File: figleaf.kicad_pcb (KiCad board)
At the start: 2 copper layers, 145 x 105 mm, 70 parts, among them J1 Conn_01x02_Pin, J2 HRO_TYPE-C-31-M-14, J3 Battery, J9 TC2030_SWD, Q2 2N7002, SW1 PWR, SW2 RST, U1 SRV05-4, U10 MAX17048, U3 BQ24075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

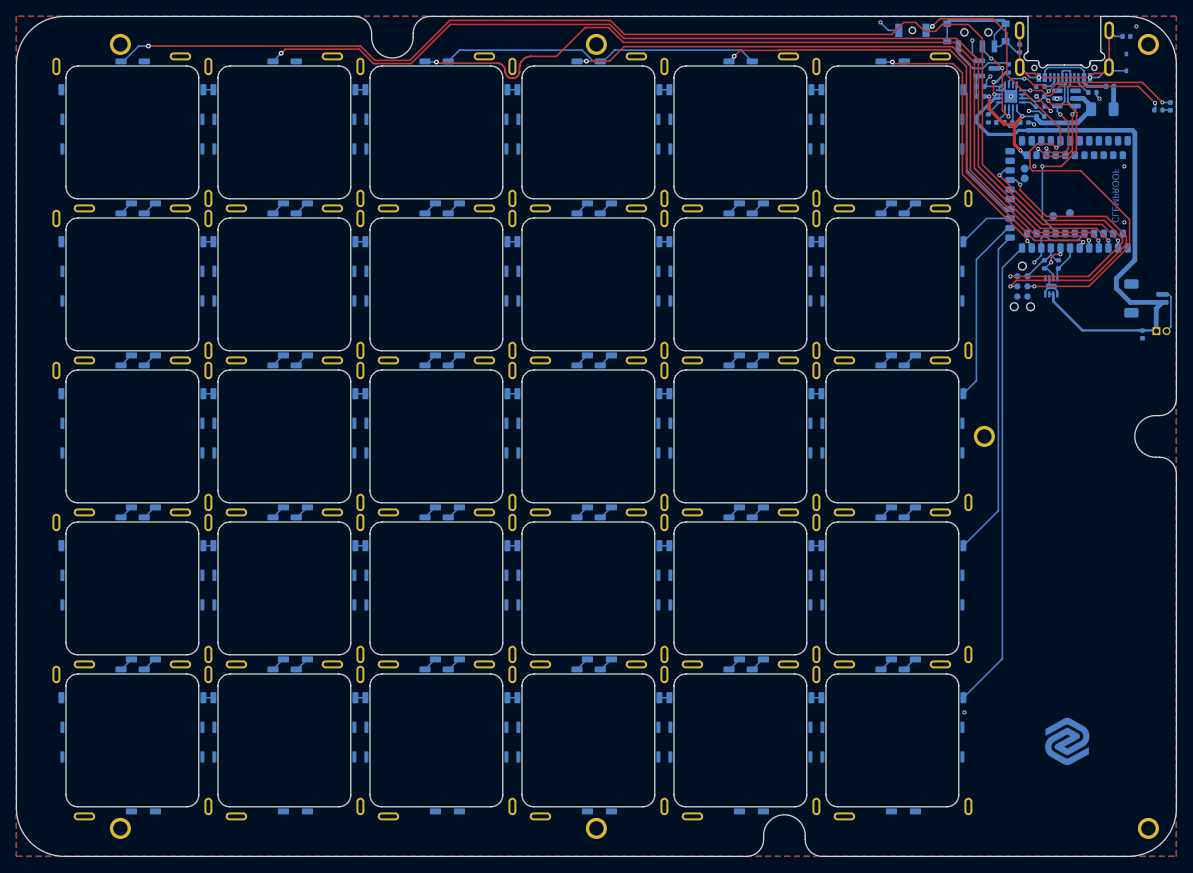
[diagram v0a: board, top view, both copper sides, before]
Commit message: data line thickness + mounting cuts
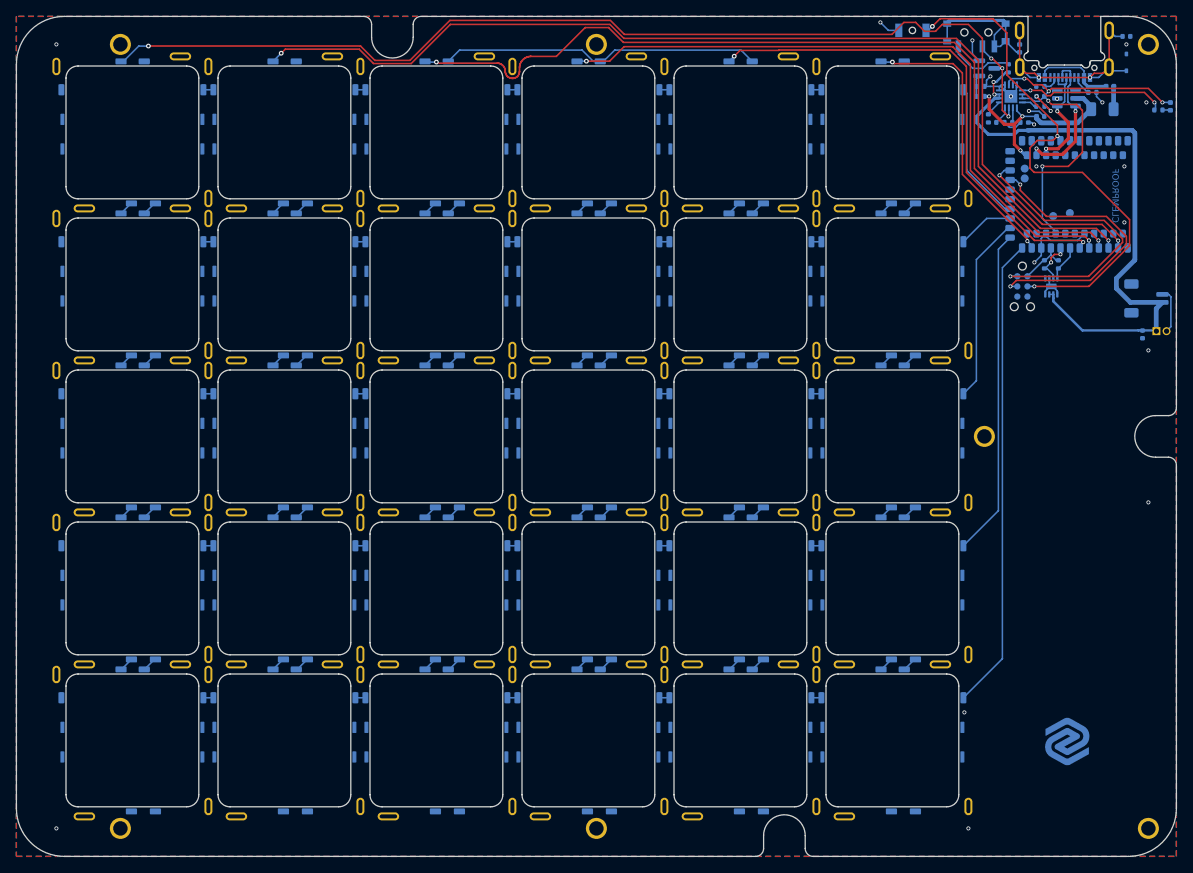
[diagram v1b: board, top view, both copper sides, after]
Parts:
- U8: footprint PCM_marbastlib-various:nRF52840_moko_mk08 -> Graz_Footprints:nRF52840_moko_mk08_GRAZ
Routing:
- net RST: track 69.2 -> 67.5 mm
- net USB-D-: track 15.9 -> 14.8 mm
- net +VSW: track 51.4 -> 52.4 mm
- net GND_L: track 105.8 -> 106.5 mm, vias 16 -> 22
- net Net-(U3-~{CHG}): track 19.2 -> 18.6 mm
- net USB-D+: track 18.6 -> 18.1 mm
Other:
- outline, holes or cut-outs redrawn

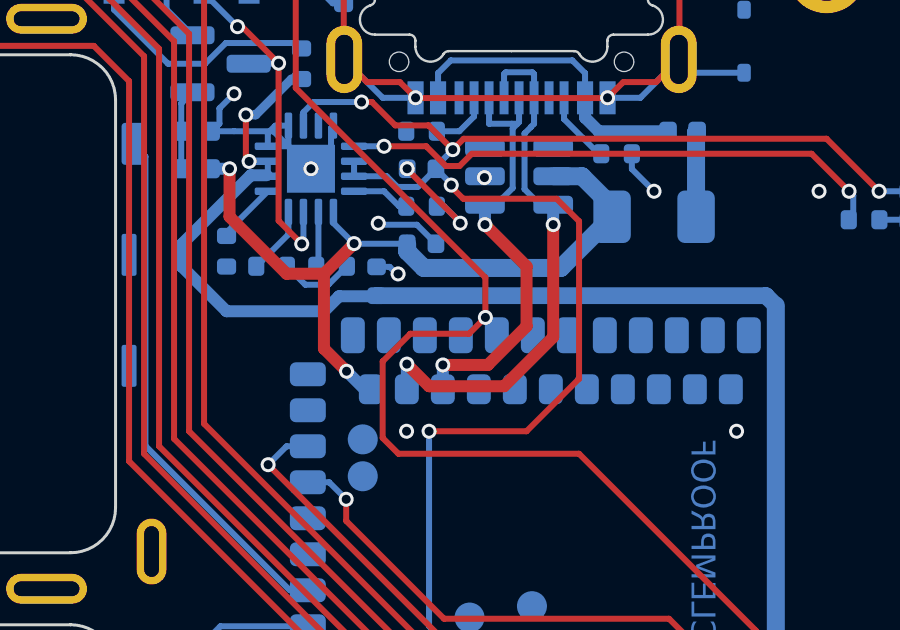
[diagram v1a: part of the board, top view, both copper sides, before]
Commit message: trace thickness saved
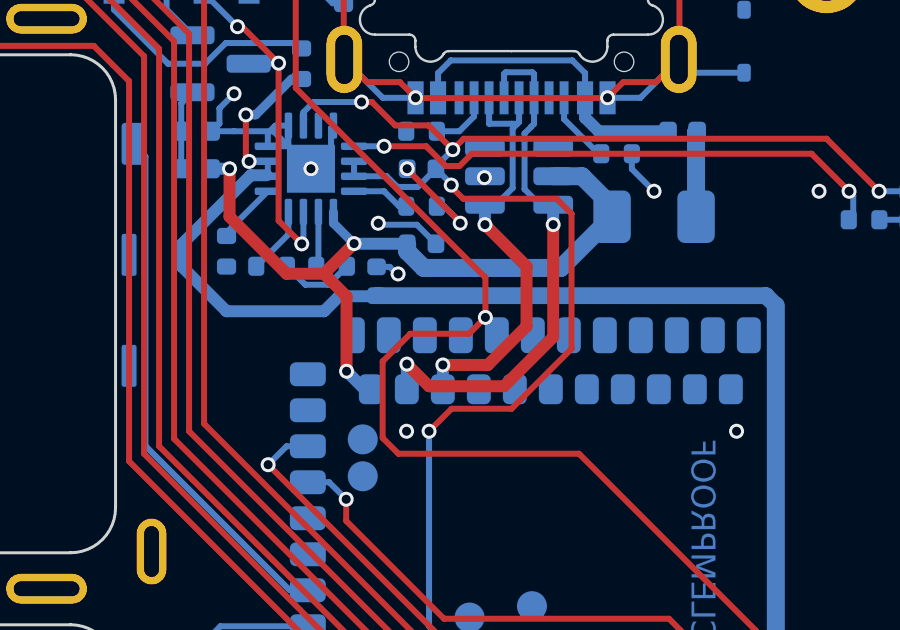
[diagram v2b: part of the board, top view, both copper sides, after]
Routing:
- net +VSW: track 52.4 -> 51.5 mm

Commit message: new bosses
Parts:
- moved J9 1.50 mm to (138.2, 47.8)
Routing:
- net col_2: track 108.4 -> 133.6 mm
- net col_3: track 83.5 -> 107.8 mm
- net col_0: track 151.8 -> 149.4 mm
- net col_4: track 63.5 -> 61.8 mm
- net +3.3V: track 6.13 -> 7.61 mm
- net col_1: track 127.7 -> 128.7 mm
- net SWDIO: track 37.4 -> 38.0 mm
- net SWDCLK: track 36.4 -> 37.0 mm
- net GND_L: track 106.5 -> 106.2 mm, vias 22 -> 26
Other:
- outline, holes or cut-outs redrawn
